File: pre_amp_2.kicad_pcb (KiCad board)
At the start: 2 copper layers, 62 x 49.3 mm, 52 parts, among them J1 IN, J10 SW2_3, J11 SW2_1, J12 SW2_4, J13 SW5_3, J14 VR5_1, J15 OUT, J16 +Led, J17 -Led, J2 Vin, J3 GND, J4 VR1_1, J5 VR2_1, J6 VR1_3, J7 VR1_2, J8 SW1, J9 SW2, U1 TL072, U2 ICL7660

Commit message: 配置をやり直す
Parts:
- removed the J16 at (162.9, 82.0)
- removed J17: -Led, Connector_PinHeader_2.54mm:PinHeader_1x01_P2.54mm_Vertical
- removed R10: 2.2k, Resistor_THT:R_Axial_DIN0204_L3.6mm_D1.6mm_P7.62mm_Horizontal
- removed R12: 10k, Resistor_THT:R_Axial_DIN0204_L3.6mm_D1.6mm_P7.62mm_Horizontal
- removed the R6 at (159.9, 82.0)
- added J2: GND2, Connector_PinHeader_2.54mm:PinHeader_1x01_P2.54mm_Vertical, F.Cu at (133.6, 80.8)
- J10: renamed from J9; value SW2 -> SW1_2
- J9: renamed from J8; value SW1 -> SW1_1
- R1, R2, R3, R4, R5: footprint Resistor_THT:R_Axial_DIN0204_L3.6mm_D1.6mm_P7.62mm_Horizontal -> Resistor_THT:R_Axial_DIN0204_L3.6mm_D1.6mm_P2.54mm_Vertical
- R6: renamed from R7; footprint Resistor_THT:R_Axial_DIN0204_L3.6mm_D1.6mm_P7.62mm_Horizontal -> Resistor_THT:R_Axial_DIN0204_L3.6mm_D1.6mm_P2.54mm_Vertical
- moved C10 56.3 mm to (117.2, 65.0), turned to -90 degrees
- moved J8 55.3 mm to (120.9, 64.3)
- moved J9 53.2 mm to (117.2, 70.6)
- moved J4 48.7 mm to (151.9, 60.2)
- moved J5 42.7 mm to (124.8, 64.3)
- moved C13 37.3 mm to (131.6, 55.4), turned to -90 degrees
- moved J13 35.2 mm to (166.1, 83.3)
- moved C3 35.2 mm to (152.7, 55.4), turned to 90 degrees
- moved C9 33.4 mm to (133.6, 46.6)
- moved R1 33.3 mm to (132.4, 74.7), turned to 180 degrees
- moved J1 32.5 mm to (129.4, 80.8)
- moved J7 32.1 mm to (128.8, 64.3)
- moved D1 31.8 mm to (162.3, 76.2)
- moved D4 31.8 mm to (154.7, 83.8)
- moved D2 31.8 mm to (154.7, 78.7)
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- renumbered D3 to D1, D4 to D2, D5 to D3, D6 to D4, J10 to J11, J11 to J12, J12 to J13, J13 to J14, J14 to J15, J15 to J16, J2 to J3, J3 to J4, J4 to J5, J5 to J6, J6 to J7, J7 to J8, R8 to R7, R9 to R8, R11 to R9
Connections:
- R1 pad 1: GND -> GND2
- R2 pad 1: GND -> GND2
- R7 pad 1: GND -> GND2
- R8 pad 1: GND -> GND2
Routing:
- net GND: track 0.00 -> 52.4 mm
- net Net-(U1C-V-): track 44.7 -> 30.5 mm
- net Net-(U1B-+): track 13.2 -> 0.00 mm
- net Net-(J11-Pin_1): track 21.8 -> 8.87 mm
- net Net-(C4-Pad1): track 16.7 -> 6.57 mm
- net Net-(U2-CAP-): track 16.6 -> 6.84 mm
- net Net-(J16-Pin_1): track 7.80 -> 0.00 mm
- net Net-(D2-K): track 3.23 -> 0.00 mm
- net Net-(C5-Pad1): track 11.1 -> 14.3 mm
- net Net-(D1-A) (its old number): track 3.05 -> 0.00 mm
- net GND2: track 0.00 -> 2.74 mm
- net Net-(J3-Pin_1): track 9.63 -> 7.01 mm
- net Net-(J7-Pin_1): track 3.60 -> 5.93 mm
- net Net-(U2-VOUT): track 14.4 -> 12.2 mm
- net Net-(U1A--): track 8.80 -> 6.91 mm
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- removed copper zone on B.Cu, net GND
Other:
- board outline removed

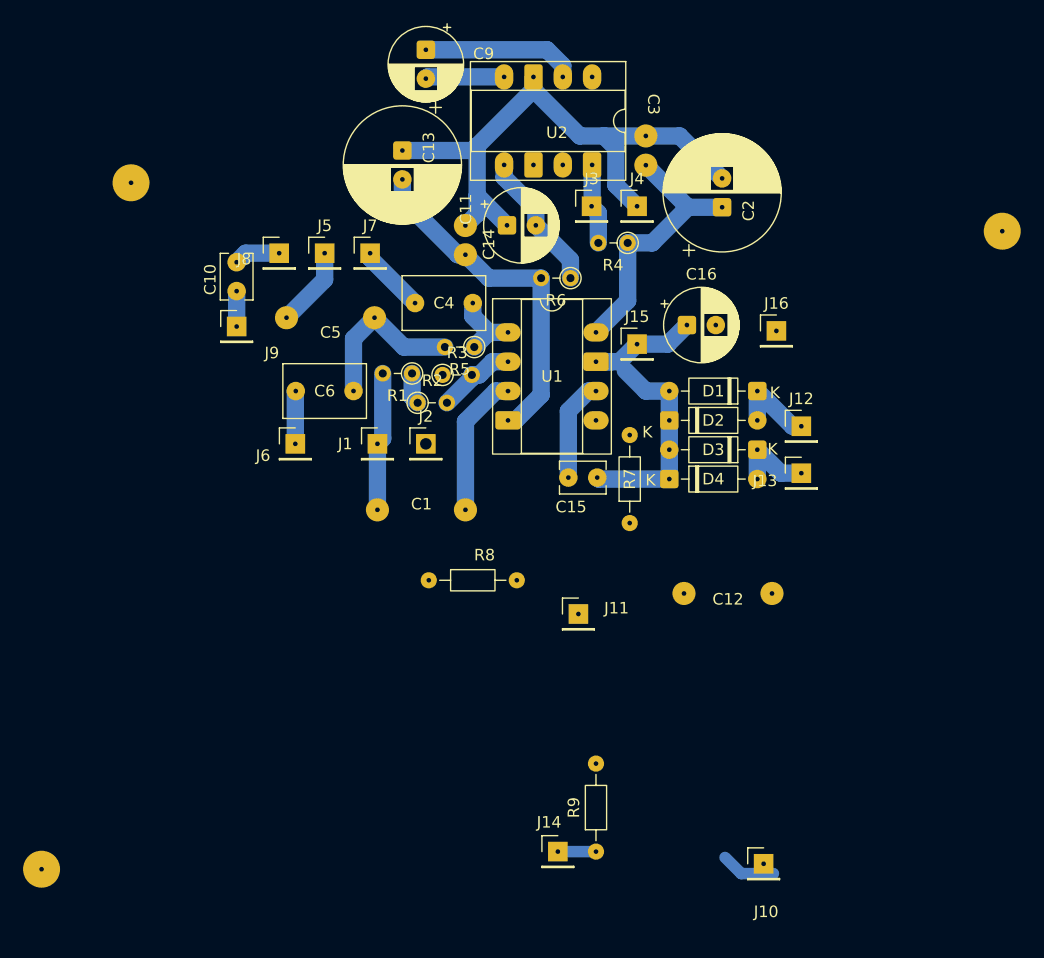
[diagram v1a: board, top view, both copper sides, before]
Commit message: 電源と入力のGNDを分離して配置を修正
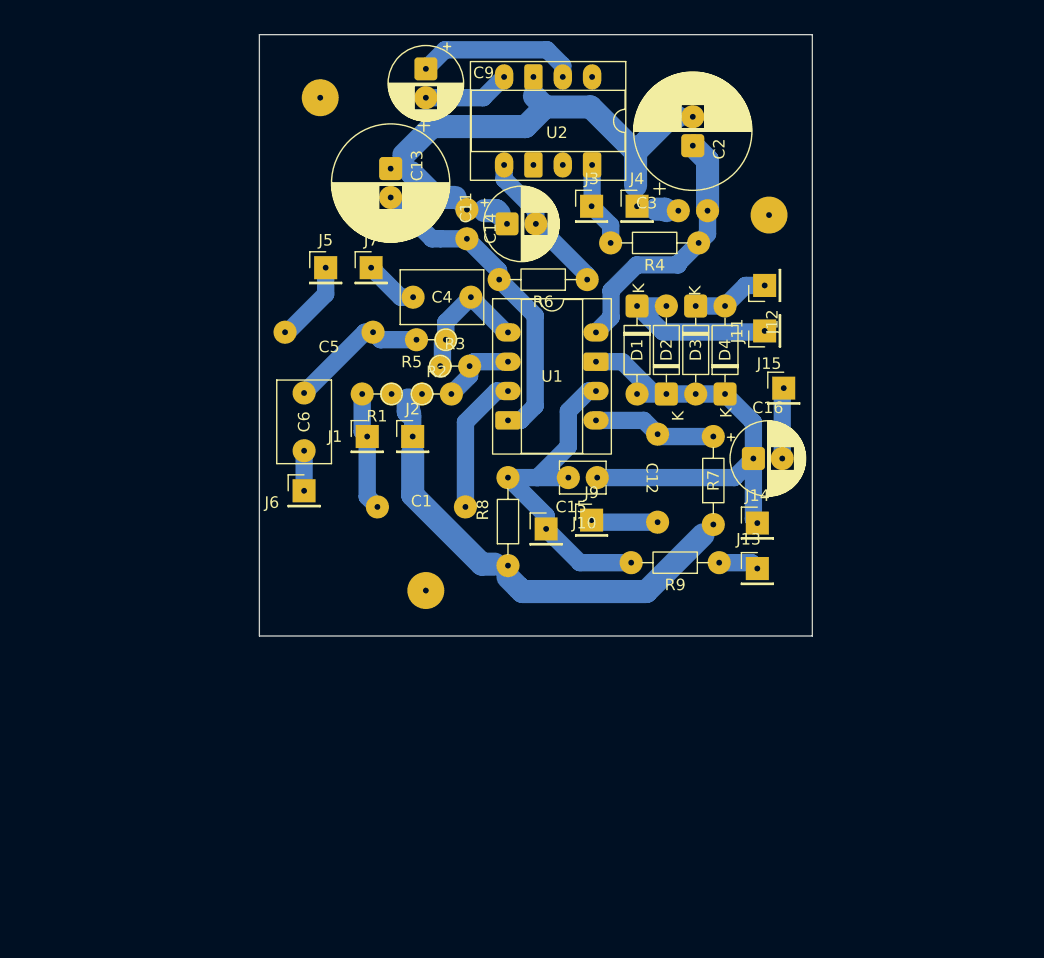
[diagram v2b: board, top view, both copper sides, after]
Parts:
- removed C10: 120p, Capacitor_THT:C_Disc_D3.8mm_W2.6mm_P2.50mm
- removed the J10 at (162.9, 117.1)
- removed J8: VR1_2, Connector_PinHeader_2.54mm:PinHeader_1x01_P2.54mm_Vertical
- J13: renamed from J14; value SW5_3 -> VR5_3
- J9: value SW1_1 -> SW1_2
- R4, R6: footprint Resistor_THT:R_Axial_DIN0204_L3.6mm_D1.6mm_P2.54mm_Vertical -> Resistor_THT:R_Axial_DIN0204_L3.6mm_D1.6mm_P7.62mm_Horizontal
- moved H3 41.1 mm to (133.6, 93.5)
- moved J9 35.0 mm to (148.0, 87.4)
- moved J13 30.0 mm to (162.3, 91.6)
- moved R9 27.2 mm to (159.0, 91.1), turned to 180 degrees
- moved H2 20.2 mm to (163.3, 61.0)
- moved J14 18.7 mm to (162.3, 87.6)
- moved H1 18.0 mm to (124.5, 50.8)
- moved J12 16.6 mm to (162.9, 67.1), turned to 90 degrees
- moved D3 13.5 mm to (157.0, 68.8), turned to -90 degrees
- moved C16 12.9 mm to (162.0, 82.0)
- moved D1 12.8 mm to (151.9, 68.8), turned to -90 degrees
- moved C12 11.7 mm to (153.7, 83.7), turned to 90 degrees
- moved J11 8.84 mm to (162.9, 71.0), turned to 90 degrees
- moved D4 8.81 mm to (159.5, 76.5), turned to 90 degrees
- moved J10 7.88 mm to (144.0, 88.1)
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- renumbered J11 to J10, J12 to J11, J13 to J12, J15 to J14, J16 to J15
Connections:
- C12 pad 1: Net-(J10-Pin_1) (its old number) -> Net-(J9-Pin_1)
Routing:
- net GND2: track 2.74 -> 38.2 mm
- net Net-(J10-Pin_1): track 8.87 -> 29.6 mm
- net Net-(D1-A): track 29.0 -> 40.0 mm
- net Net-(U1B-+): track 0.00 -> 10.7 mm
- net Net-(D1-K): track 7.61 -> 14.6 mm
- net Net-(J15-Pin_1): track 0.00 -> 6.15 mm
- net GND: track 52.4 -> 46.3 mm
- net Net-(C4-Pad1): track 6.57 -> 11.5 mm
- net Net-(J10-Pin_1) (its old number): track 4.77 -> 0.00 mm
- net Net-(J8-Pin_1): track 4.01 -> 0.00 mm
- net Net-(U1C-V-): track 30.5 -> 27.6 mm
- net Net-(J9-Pin_1): track 3.07 -> 5.79 mm
- net Net-(C5-Pad1): track 14.3 -> 12.2 mm
- net Net-(J1-Pin_1): track 12.0 -> 10.3 mm
- net Net-(J7-Pin_1): track 5.93 -> 4.69 mm
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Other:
- board outline added: 47.9 x 52.1 mm

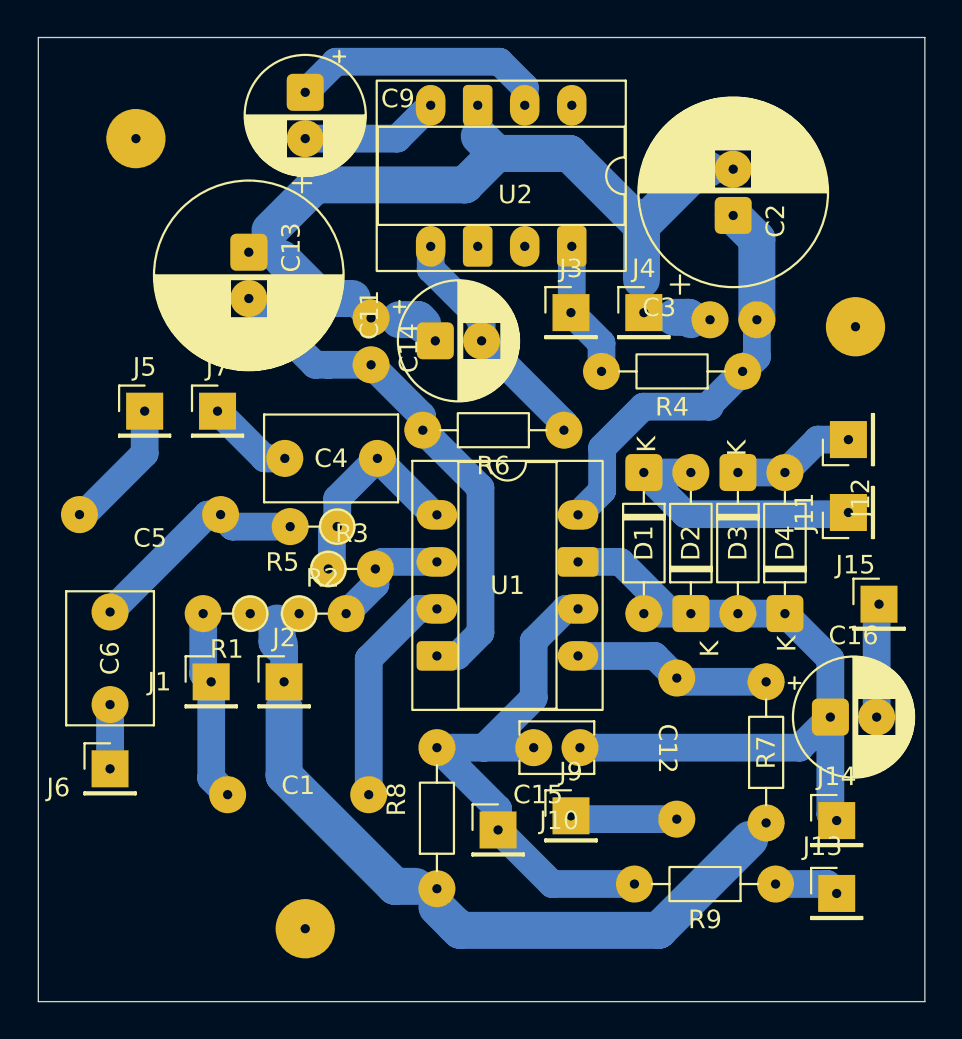
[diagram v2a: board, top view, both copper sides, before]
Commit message: パッドの大きさを大きくした
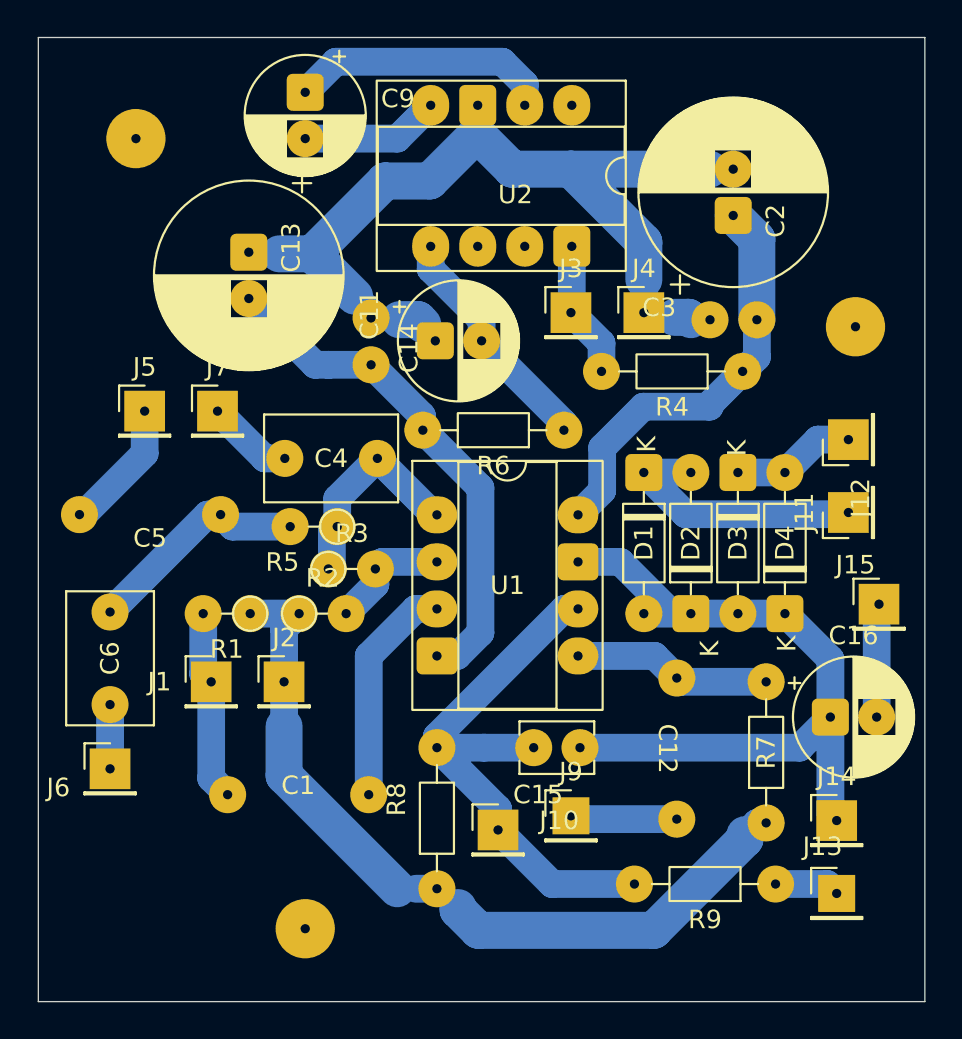
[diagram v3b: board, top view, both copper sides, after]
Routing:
- net GND2: track 38.2 -> 41.3 mm
- net Net-(J10-Pin_1): track 29.6 -> 30.7 mm
- net GND: track 46.3 -> 45.4 mm

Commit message: 配線の接続先を修正
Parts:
- J6: value VR2_1 -> VR3_3
- J9: value SW1_2 -> VR4_2

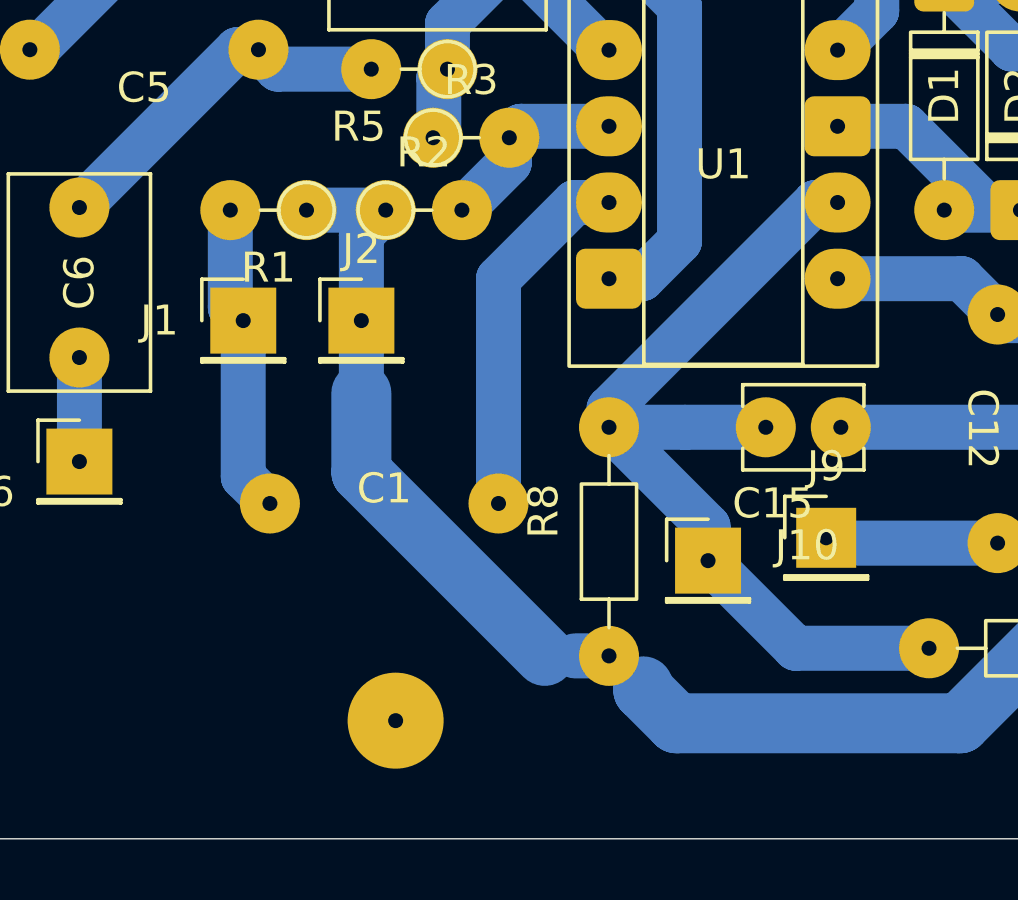
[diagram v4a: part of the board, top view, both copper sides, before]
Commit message: ICにパスコンを付けるためGND2を近づけた
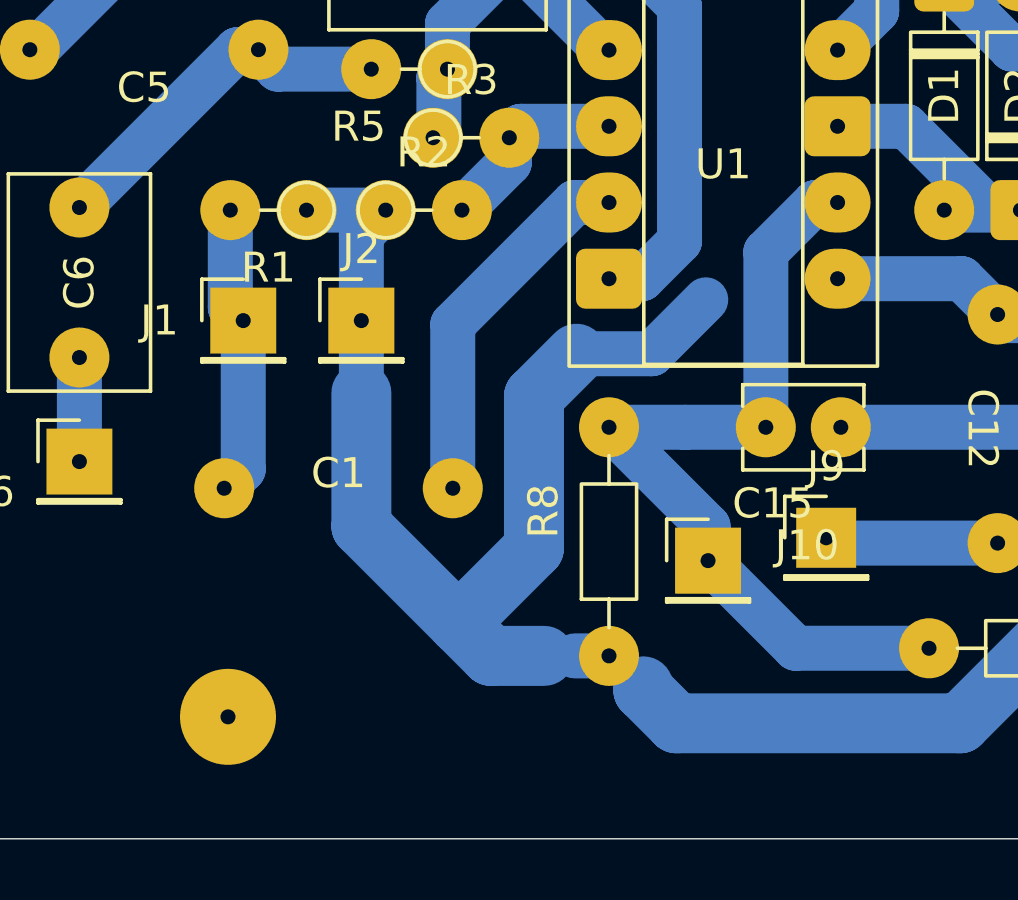
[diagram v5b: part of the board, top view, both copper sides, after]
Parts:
- moved H3 5.59 mm to (128.0, 93.3)
- moved C1 1.61 mm to (131.7, 85.7)
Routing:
- net GND2: track 41.3 -> 58.0 mm
- net Net-(J10-Pin_1): track 30.7 -> 28.5 mm
- net Net-(J1-Pin_1): track 10.3 -> 9.71 mm
